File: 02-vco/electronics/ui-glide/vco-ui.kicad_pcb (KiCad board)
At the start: 2 copper layers, 58 x 110 mm, 40 parts, among them J1 Conn_01x04, J2 Conn_02x05_Odd_Even, J3 Conn_02x03_Odd_Even, J4 Conn_01x02, J5 Conn_02x02_Counter_Clockwise, J6 Conn_01x07, U1 0203

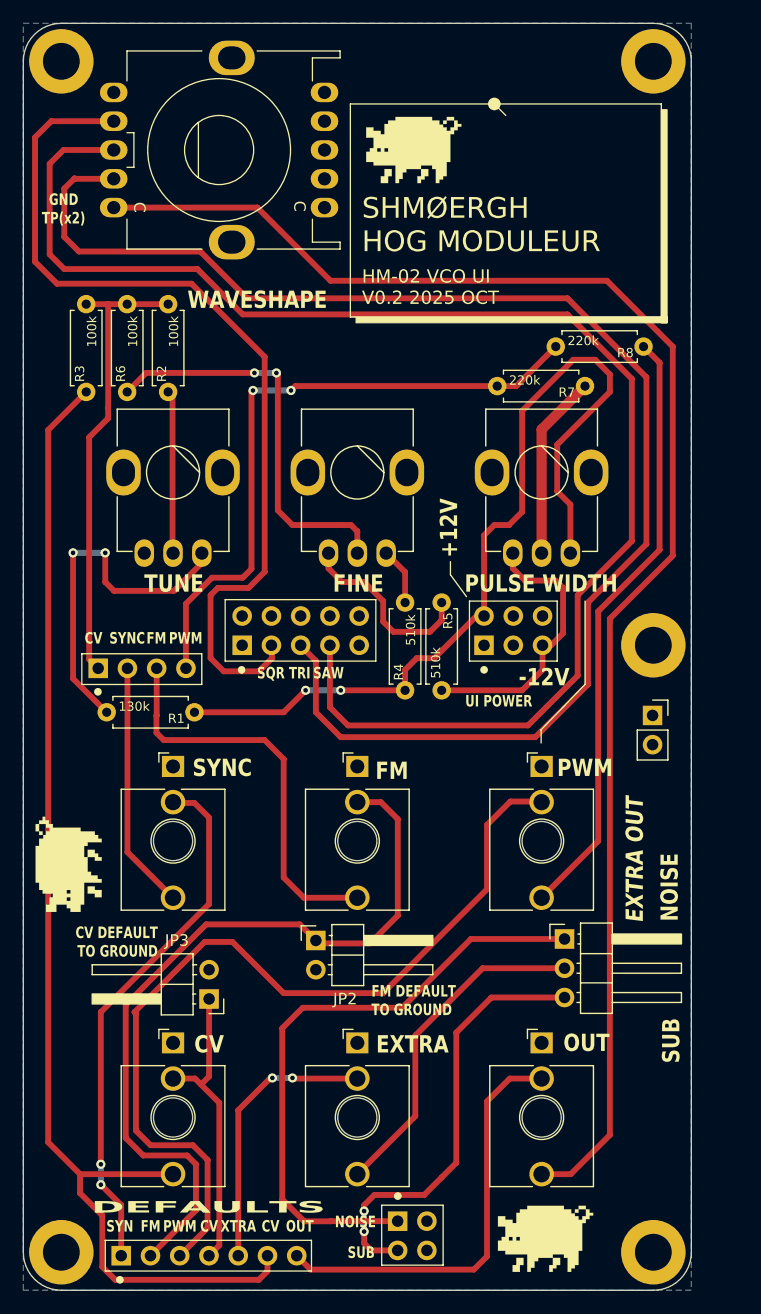
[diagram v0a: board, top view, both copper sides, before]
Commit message: Added Glided VCO UI PCB
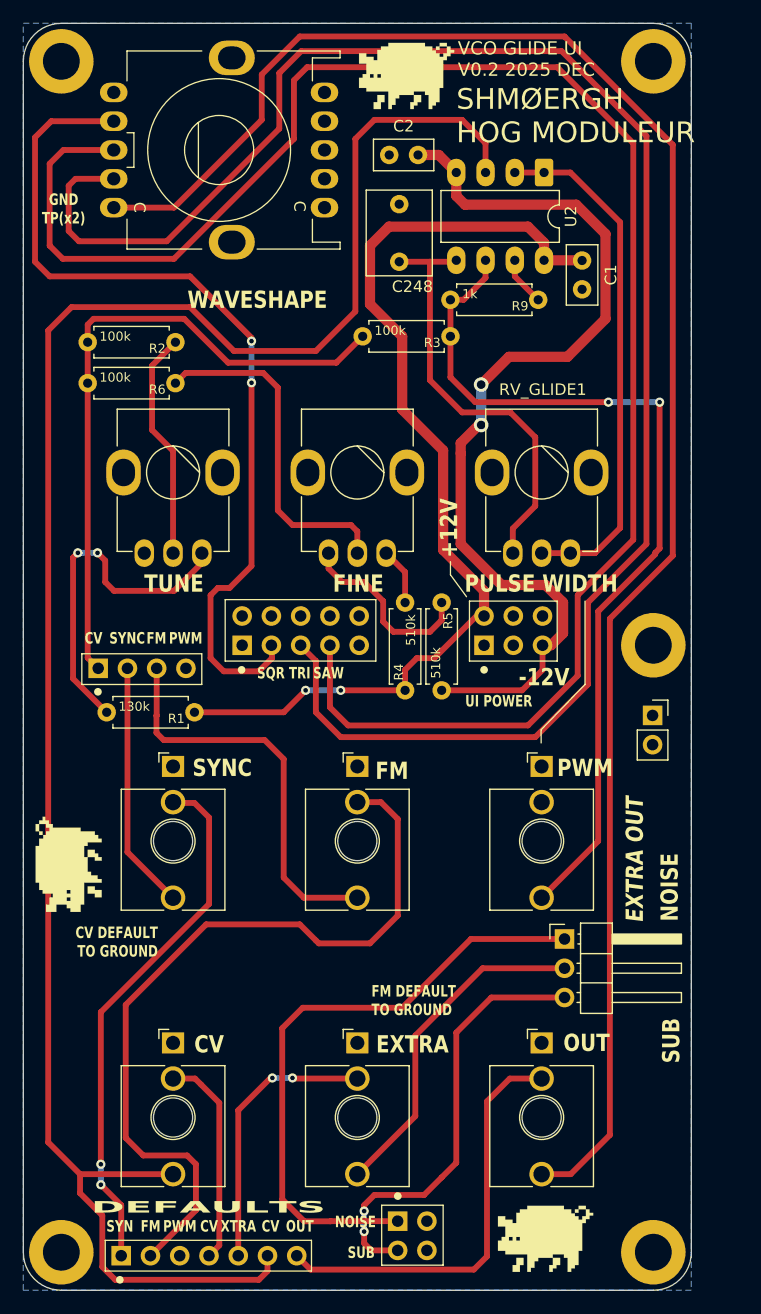
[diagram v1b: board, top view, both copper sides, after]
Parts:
- removed JP2, JP3: Jumper_2_Open, Connector_PinHeader_2.54mm:PinHeader_1x02_P2.54mm_Horizontal
- removed J_PWM1: PJ398SM, Shmoergh_Custom_Footprints:Jack_3.5mm_QingPu_WQP-PJ398SM_Vertical_CircularHoles
- removed R7, R8: 220k, Shmoergh_Custom_Footprints:R_Axial_DIN0207_L6.3mm_D2.5mm_P7.62mm_Horizontal
- removed RV_PWM1: 100k, Shmoergh_Custom_Footprints:Potentiometer_Bourns_Single-PTV09A
- added C1: 100n, Capacitor_THT:C_Disc_D5.0mm_W2.5mm_P2.50mm, F.Cu at (172.5, 64.6)
- added C2: 100n, Capacitor_THT:C_Disc_D5.0mm_W2.5mm_P2.50mm, F.Cu at (155.8, 55.4)
- added C248: 1u (foil or electrolite), Capacitor_THT:C_Rect_L7.2mm_W5.5mm_P5.00mm_FKS2_FKP2_MKS2_MKP2, F.Cu at (156.6, 64.7)
- added J_GLIDED_PITCH_OUT1: PJ398SM, Shmoergh_Custom_Footprints:Jack_3.5mm_QingPu_WQP-PJ398SM_Vertical_CircularHoles, F.Cu at (169.0, 115.0)
- added R9: 1k, Shmoergh_Custom_Footprints:R_Axial_DIN0207_L6.3mm_D2.5mm_P7.62mm_Horizontal, F.Cu at (168.7, 68.0)
- added RV_GLIDE1: 100k, Shmoergh_Custom_Footprints:Potentiometer_Bourns_Single-PTV09A, F.Cu at (169.0, 83.0)
- added U2: TL072, Package_DIP:DIP-8_W7.62mm_LongPads, F.Cu at (169.2, 57.0)
- moved R3 32.0 mm to (161.1, 71.2), turned to 180 degrees
- moved G*** 9.91 mm to (169.0, 73.3)
- moved G*** 7.48 mm to (167.8, 50.4)
- moved G*** 6.46 mm to (157.3, 48.6)
- moved R2 4.36 mm to (137.2, 71.7), turned to 180 degrees
- moved R6 4.26 mm to (137.2, 75.2), turned to 180 degrees
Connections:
- R3 pad 1: CV_INPUT -> Net-(U2B--)
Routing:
- net Net-(U2B--): track 0.00 -> 78.4 mm, vias 0 -> 2
- net PWM_DEFAULT: track 76.8 -> 0.00 mm
- net CV_INPUT: track 103.8 -> 168.6 mm
- net -12V: track 24.2 -> 83.0 mm, vias 0 -> 2
- net SQR_SHAPE: track 56.0 -> 0.00 mm, vias 2 -> 0
- net Net-(J_PWM1-PadT): track 52.7 -> 0.00 mm
- net Net-(U2A--): track 0.00 -> 45.2 mm
- net Net-(U2B-+): track 0.00 -> 37.4 mm
- net SAW: track 126.0 -> 154.4 mm
- net TRI: track 126.0 -> 153.8 mm
- net Net-(J_OUT1-PadT): track 131.6 -> 156.5 mm
- net CV: track 39.7 -> 56.8 mm
- net Net-(R7-Pad1): track 16.1 -> 0.00 mm
- net +12V: track 77.4 -> 87.1 mm
- net CV_DEFAULT: track 26.3 -> 18.5 mm
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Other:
- board text added: "VCO GLIDE UI V0.2 2025 DEC"
- board text removed: "HM-02 VCO UI V0.2 2025 OCT"
